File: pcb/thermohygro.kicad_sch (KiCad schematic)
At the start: 5 parts, among them J1 RJ45_Shielded, J2 RJ45_Shielded, J3 SSD1306, U1 XIAO-ESP32-S3

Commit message: schematics v0.9 pdf
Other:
- title: (none) -> Thermohygro
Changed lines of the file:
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@@
 	(generator_version "10.0")
 	(paper "A4")
+	(title_block
+		(title "Thermohygro")
+		(rev "0.9")
+	)
 	(junction
 		(at 132.08 72.39)

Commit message: closer RJ45
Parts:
- J1, J2: footprint Connector_RJ:RJ45_HALO_HFJ11-x2450HRL_Horizontal -> rj45:RJ45_HALO_HFJ11-x2450HRL_Horizontal_closer
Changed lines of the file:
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@@
 			)
 		)
-		(property "Footprint" "Connector_RJ:RJ45_HALO_HFJ11-x2450HRL_Horizontal"
+		(property "Footprint" "rj45:RJ45_HALO_HFJ11-x2450HRL_Horizontal_closer"
 			(at 132.715 48.26 90)
 			(hide yes)
@@
 			)
 		)
-		(property "Footprint" "Connector_RJ:RJ45_HALO_HFJ11-x2450HRL_Horizontal"
+		(property "Footprint" "rj45:RJ45_HALO_HFJ11-x2450HRL_Horizontal_closer"
 			(at 102.235 48.26 90)
 			(hide yes)

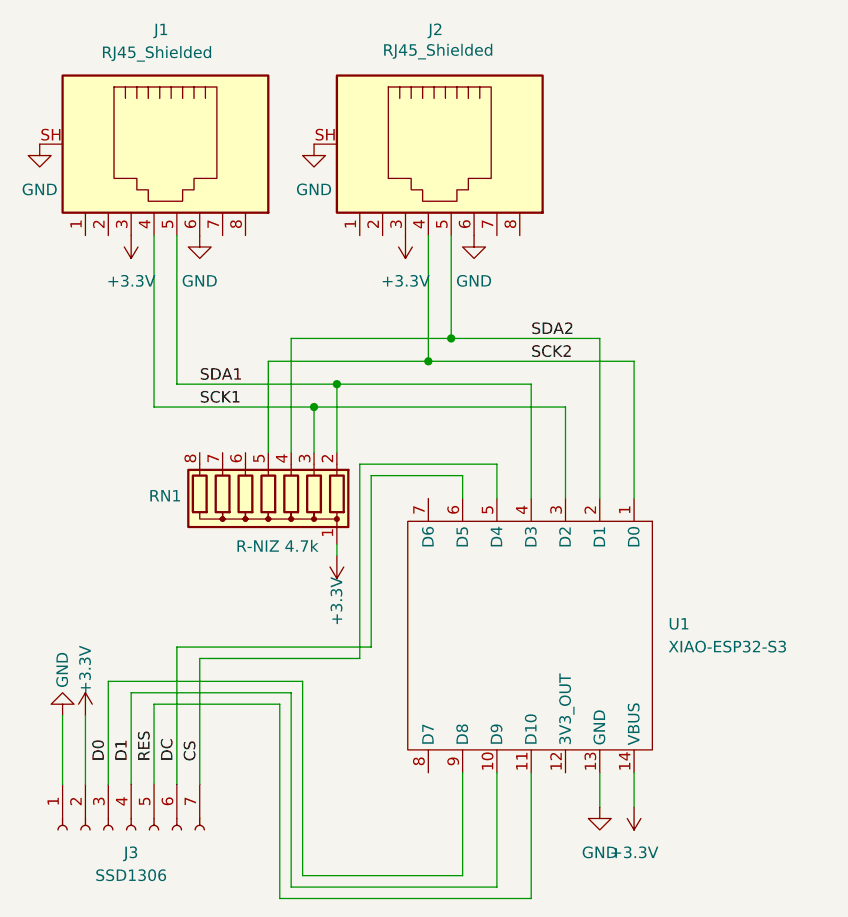
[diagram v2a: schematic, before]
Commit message: pullup for display i2c
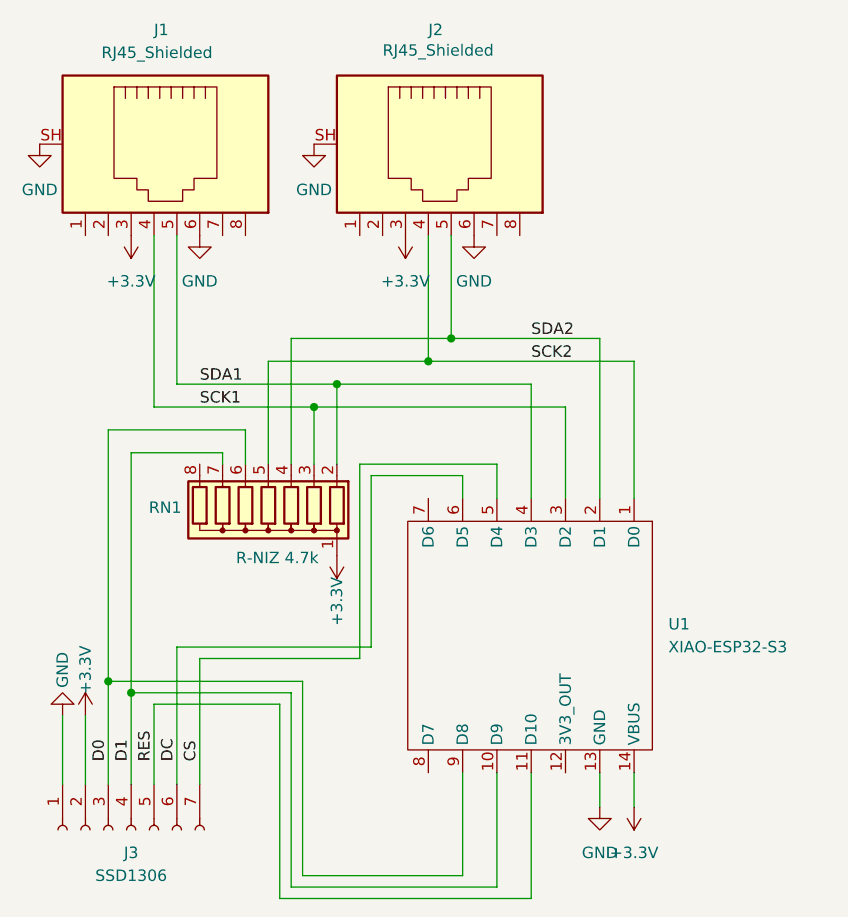
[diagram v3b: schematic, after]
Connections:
- net D0: now also RN1.6 (R5)
- net D1: now also RN1.7 (R6)
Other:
- moved on the sheet: RN1
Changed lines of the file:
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@@
+	)
+	(junction
+		(at 96.52 107.95)
+		(diameter 0)
+		(color 0 0 0 0)
 	)
 	(junction
@@
 	)
 	(junction
-		(at 119.38 77.47)
-		(diameter 0)
-		(color 0 0 0 0)
-	)
-	(junction
 		(at 121.92 74.93)
 		(diameter 0)
@@
 		(color 0 0 0 0)
 	)
+	(junction
+		(at 119.38 77.47)
+		(diameter 0)
+		(color 0 0 0 0)
+	)
+	(junction
+		(at 99.06 109.22)
+		(diameter 0)
+		(color 0 0 0 0)
+	)
 	(wire
 		(pts
@@
 	(wire
 		(pts
-			(xy 121.92 93.98) (xy 121.92 92.71)
-		)
-		(stroke
-			(width 0)
-			(type default)
-		)
-	)
-	(wire
-		(pts
-			(xy 116.84 82.55) (xy 116.84 69.85)
+			(xy 116.84 83.82) (xy 116.84 69.85)
 		)
 		(stroke
@@
 	(wire
 		(pts
+			(xy 111.76 80.01) (xy 111.76 83.82)
+		)
+		(stroke
+			(width 0)
+			(type default)
+		)
+	)
+	(wire
+		(pts
 			(xy 143.51 118.11) (xy 143.51 132.08)
 		)
@@
 	(wire
 		(pts
-			(xy 119.38 77.47) (xy 119.38 82.55)
+			(xy 119.38 77.47) (xy 119.38 83.82)
 		)
 		(stroke
@@
 	(wire
 		(pts
+			(xy 99.06 82.55) (xy 109.22 82.55)
+		)
+		(stroke
+			(width 0)
+			(type default)
+		)
+	)
+	(wire
+		(pts
 			(xy 139.7 83.82) (xy 139.7 87.63)
 		)
@@
 	(wire
 		(pts
+			(xy 109.22 82.55) (xy 109.22 83.82)
+		)
+		(stroke
+			(width 0)
+			(type default)
+		)
+	)
+	(wire
+		(pts
+			(xy 99.06 109.22) (xy 99.06 82.55)
+		)
+		(stroke
+			(width 0)
+			(type default)
+		)
+	)
+	(wire
+		(pts
+			(xy 96.52 80.01) (xy 111.76 80.01)
+		)
+		(stroke
+			(width 0)
+			(type default)
+		)
+	)
+	(wire
+		(pts
 			(xy 106.68 105.41) (xy 106.68 119.38)
 		)
@@
 	(wire
 		(pts
-			(xy 114.3 82.55) (xy 114.3 72.39)
+			(xy 114.3 83.82) (xy 114.3 72.39)
 		)
 		(stroke
@@
 	(wire
 		(pts
+			(xy 96.52 107.95) (xy 96.52 80.01)
+		)
+		(stroke
+			(width 0)
+			(type default)
+		)
+	)
+	(wire
+		(pts
 			(xy 121.92 74.93) (xy 143.51 74.93)
 		)
@@
 	(wire
 		(pts
-			(xy 121.92 82.55) (xy 121.92 74.93)
+			(xy 121.92 83.82) (xy 121.92 74.93)
 		)
 		(stroke
@@
 	(symbol
 		(lib_id "Device:R_Network07")
-		(at 114.3 87.63 180)
+		(at 114.3 88.9 180)
 		(unit 1)
 		(body_style 1)
@@
 		(dnp no)
 		(property "Reference" "RN1"
-			(at 104.648 87.376 0)
+			(at 104.648 88.646 0)
 			(show_name no)
 			(do_not_autoplace no)
@@
 		)
 		(property "Value" "R-NIZ 4.7k"
-			(at 119.888 92.964 0)
+			(at 119.888 94.234 0)
 			(show_name no)
 			(do_not_autoplace no)
@@
 		)
 		(property "Footprint" "Resistor_THT:R_Array_SIP8"
-			(at 102.235 87.63 90)
+			(at 102.235 88.9 90)
 			(hide yes)
 			(show_name no)
@@
 		)
 		(property "Datasheet" "http://www.vishay.com/docs/31509/csc.pdf"
-			(at 114.3 87.63 0)
+			(at 114.3 88.9 0)
 			(hide yes)
 			(show_name no)
@@
 		)
 		(property "Description" "7 resistor network, star topology, bussed resistors, small symbol"
-			(at 114.3 87.63 0)
-			(hide yes)
-			(show_name no)
+			(at 114.3 88.9 0)
+			(hide yes)
+			(show_name no)
